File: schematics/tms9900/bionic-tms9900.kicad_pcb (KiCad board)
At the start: 4 copper layers, 30.5 x 88.9 mm, 35 parts, among them J1 Bionic-P135, J2 Bionic-P245, Q1 2N7002DW, Q2 2N7002DW, U1 TMS9900, U2 11AA010-I/TT, U3 74ACT157, U4 74ACT157, U5 74HCT259, U6 74ACT164, U7 LM2776, U8 NJW4132

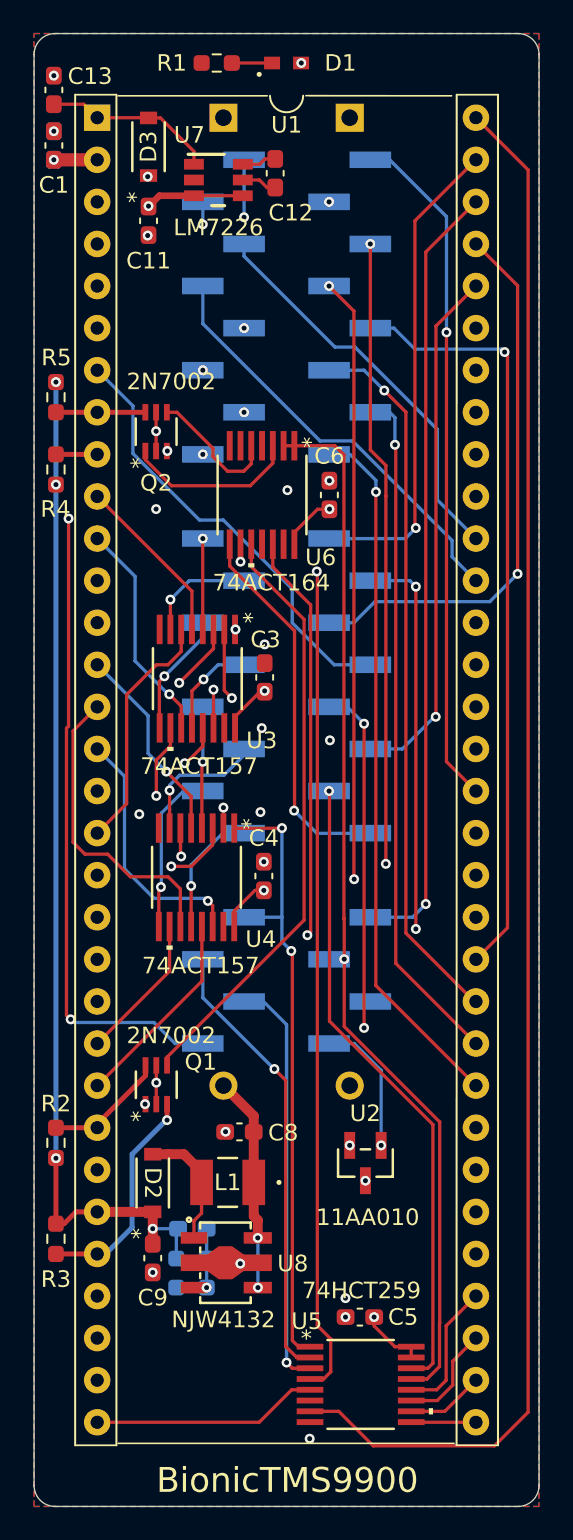
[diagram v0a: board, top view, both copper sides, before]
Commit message: [schematics] Straighten board tracks and regenerate Gerbers
straighten_tracks.py on every routed board: router leftovers snapped to
0/45/90 degrees and redundant segments merged, each pass DRC-checked
(counts unchanged). Gerbers and drill files of the changed boards are
regenerated with each board's plot settings, keeping the committed file
sets; tms9980 keeps its tracks (the rebuild left a dangling VCC stub).
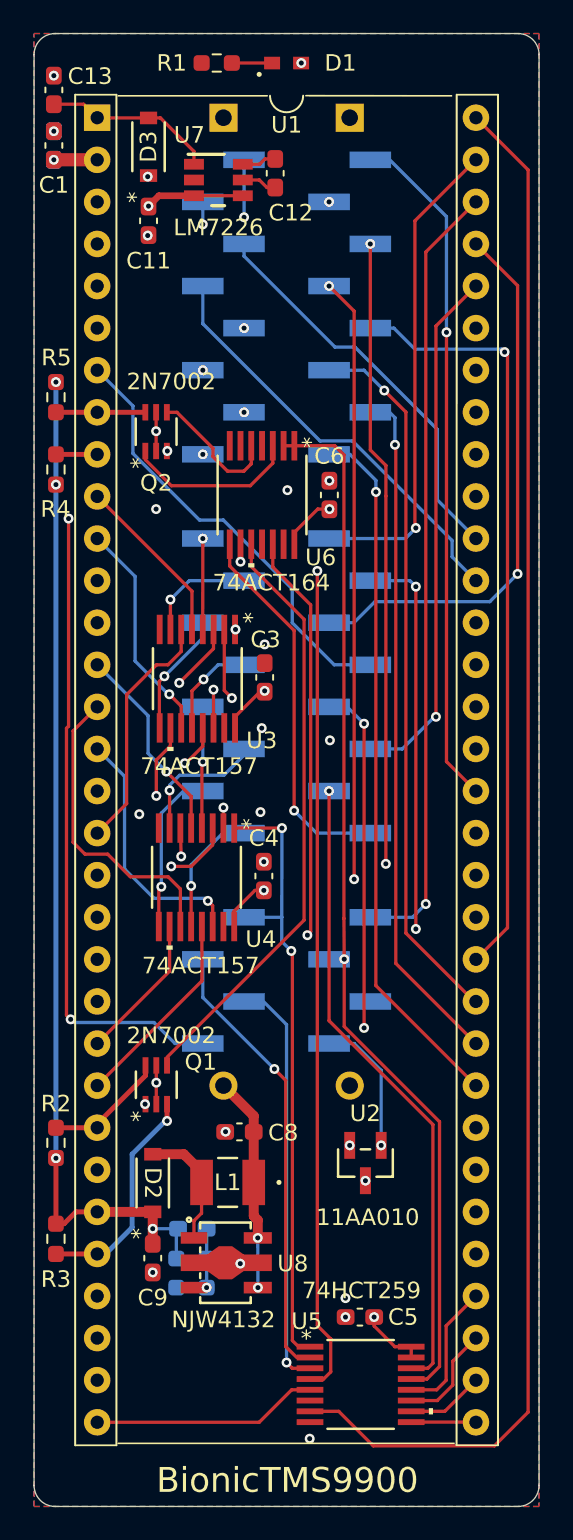
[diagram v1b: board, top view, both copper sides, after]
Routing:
- net VCC: track 41.2 -> 39.4 mm
- net Net-(D2-A): track 8.82 -> 7.25 mm
- net Net-(U8-IN-): track 4.32 -> 3.15 mm
- net /P36: track 9.96 -> 8.79 mm
- net /P52: track 25.1 -> 23.9 mm
- net /P26: track 41.4 -> 40.3 mm
- net /P20: track 41.4 -> 40.3 mm
- net /P44: track 48.8 -> 47.7 mm
- net /P51: track 27.2 -> 26.4 mm
- net /Q0: track 75.8 -> 75.1 mm
- net /P50: track 50.7 -> 50.0 mm

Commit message: [schematics] Align silkscreen reference labels
align_silk.py snaps each footprint kind's labels onto their common
offset and angle and clears labels DRC flags on silkscreen; 76 labels on
22 boards, no DRC count grows. Their Gerbers are regenerated.
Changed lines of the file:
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@@
 		(tags "capacitor handsolder")
 		(property "Reference" "C11"
-			(at 2.413 0 180)
+			(at 2.4 0 180)
 			(layer "F.SilkS")
 			(effects
@@
 		(tags "capacitor handsolder")
 		(property "Reference" "C9"
-			(at 2.3887 0 180)
+			(at 2.4 0 180)
 			(layer "F.SilkS")
 			(effects
@@
 		(tags "capacitor handsolder")
 		(property "Reference" "C8"
-			(at -2.6405 -0.0508 0)
+			(at -2.62 -0.03 0)
 			(layer "F.SilkS")
 			(effects
@@
 		(tags "capacitor handsolder")
 		(property "Reference" "C5"
-			(at -2.6098 0 0)
+			(at -2.62 -0.03 0)
 			(layer "F.SilkS")
 			(effects

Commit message: [schematics] Remove the JLC order-number marker from all boards
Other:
- board text removed: "JLCJLCJLCJLC"
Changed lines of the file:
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@@
-		)
-	)
-	(gr_text "JLCJLCJLCJLC"
-		(at 100.33 125.5904 -0)
-		(layer "B.SilkS")
-		(effects
-			(font
-				(size 0.8 0.8)
-				(thickness 0.1)
-			)
-			(justify bottom mirror)
 		)
 	)
